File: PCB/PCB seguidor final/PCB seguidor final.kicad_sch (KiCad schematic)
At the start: 37 parts, among them J2 MOTOR A, J3 MOTOR B, J4 Conn_01x08, J6 Conn_01x04, SW1 SW_SPDT, U2 ESP32-DEVKIT-V1, U3 LM7805, U4 ROB-14450, U5 ROB-14450, U6 module_mpu6050

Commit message: las huellas FUNCIONAN
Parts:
- .1: footprint Connector:JWT_A3963_1x02_P3.96mm_Vertical -> Connector_AMASS:AMASS_XT30U-F_1x02_P5.0mm_Vertical
- R1, R2, R3, R4: footprint digikey-footprints:0603 -> digikey-kicad-library-master:0603
- U1, U7: footprint misc_footprints:MT3608_module -> MT3608:MT3608-Module

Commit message: Acabada(esperando corrección)
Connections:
- net +5V: now also GND1.3 (Pin_3)
- net +7.5V: now also SW1.1 (A)
- net BTN 1: now also U2.17 (VP); no longer U2.12 (RX0)
- net BTN 2: now also U2.12 (RX0); no longer U2.13 (TX0)
- net BTN 4: now also U2.13 (TX0); no longer U2.17 (VP)
- net MOTOR B1: now also U2.21 (D32); no longer U2.22 (D33)
- net MOTOR B2: now also U2.22 (D33); no longer U2.21 (D32)
- net VCC: no longer GND1.3 (Pin_3)
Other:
- moved on the sheet: .1
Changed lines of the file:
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@@
 	)
 	(junction
+		(at 88.9 83.82)
+		(diameter 0)
+		(color 0 0 0 0)
+	)
+	(junction
 		(at 250.19 105.41)
 		(diameter 0)
@@
 	(wire
 		(pts
-			(xy 252.73 107.95) (xy 257.81 107.95)
+			(xy 252.73 107.95) (xy 266.7 107.95)
 		)
 		(stroke
@@
 	(wire
 		(pts
+			(xy 88.9 81.28) (xy 88.9 83.82)
+		)
+		(stroke
+			(width 0)
+			(type default)
+		)
+	)
+	(wire
+		(pts
 			(xy 271.78 134.62) (xy 274.32 134.62)
 		)
@@
 	(wire
 		(pts
+			(xy 88.9 83.82) (xy 100.33 83.82)
+		)
+		(stroke
+			(width 0)
+			(type default)
+		)
+	)
+	(wire
+		(pts
 			(xy 67.31 40.64) (xy 67.31 44.45)
 		)
@@
 	(wire
 		(pts
-			(xy 250.19 105.41) (xy 257.81 105.41)
+			(xy 250.19 105.41) (xy 266.7 105.41)
 		)
 		(stroke
@@
 		)
 	)
-	(global_label "BTN 1"
+	(global_label "BTN 2"
 		(shape input)
 		(at 27.94 83.82 180)
@@
 		)
 	)
-	(global_label "BTN 2"
+	(global_label "BTN 4"
 		(shape input)
 		(at 27.94 86.36 180)
@@
 		)
 	)
-	(global_label "MOTOR B1"
+	(global_label "MOTOR B2"
 		(shape output)
 		(at 27.94 114.3 180)
@@
 		)
 	)
-	(global_label "MOTOR B2"
+	(global_label "MOTOR B1"
 		(shape output)
 		(at 27.94 111.76 180)
@@
 		)
 	)
-	(global_label "BTN 4"
+	(global_label "BTN 1"
 		(shape input)
 		(at 58.42 83.82 0)
@@
 		(on_board yes)
 		(dnp no)
-		(fields_autoplaced yes)
 		(property "Reference" "#PWR028"
 			(at 247.65 109.22 0)
@@
 		)
 		(property "Value" "+7.5V"
-			(at 247.65 100.33 0)
+			(at 247.396 101.6 0)
 			(effects
 				(font
 					(size 1.27 1.27)
 				)
+				(justify left)
 			)
 		)
@@
 	)
 	(symbol
+		(lib_id "power:+7.5V")
+		(at 88.9 83.82 0)
+		(unit 1)
+		(exclude_from_sim no)
+		(in_bom yes)
+		(on_board yes)
+		(dnp no)
+		(property "Reference" "#PWR030"
+			(at 88.9 87.63 0)
+			(effects
+				(font
+					(size 1.27 1.27)
+				)
+				(hide yes)
+			)
+		)
+		(property "Value" "+7.5V"
+			(at 88.646 80.01 0)
+			(effects
+				(font
+					(size 1.27 1.27)
+				)
+				(justify left)
+			)
+		)
+		(property "Footprint" ""
+			(at 88.9 83.82 0)
+			(effects
+				(font
+					(size 1.27 1.27)
+				)
+				(hide yes)
+			)
+		)
+		(property "Datasheet" ""
+			(at 88.9 83.82 0)
+			(effects
+				(font
+					(size 1.27 1.27)
+				)
+				(hide yes)
+			)
+		)
+		(property "Description" "Power symbol creates a global label with name \"+7.5V\""
+			(at 88.9 83.82 0)
+			(effects
+				(font
+					(size 1.27 1.27)
+				)
+				(hide yes)
+			)
+		)
+		(pin "1"
+		)
+		(instances
+			(project "PCB seguidor final"
+				(path "/e648e1de-53d7-47b7-8bc3-d4f3366b9377"
+					(reference "#PWR030")
+					(unit 1)
+				)
+			)
+		)
+	)
+	(symbol
 		(lib_id "ROB-14450:ROB-14450")
 		(at 46.99 41.91 0)
@@
 	(symbol
 		(lib_id "XT30PW-M:XT30PW-M")
-		(at 262.89 105.41 0)
+		(at 271.78 105.41 0)
 		(mirror y)
 		(unit 1)
@@
 		(dnp no)
 		(property "Reference" ".1"
-			(at 266.7 97.79 0)
+			(at 275.59 97.79 0)
 			(effects
 				(font
@@
 		)
 		(property "Value" "XT30PW-M"
-			(at 266.7 100.33 0)
+			(at 275.59 100.33 0)
 			(effects
 				(font
@@
 		)
 		(property "Footprint" "Connector_AMASS:AMASS_XT30U-F_1x02_P5.0mm_Vertical"
-			(at 262.89 105.41 0)
+			(at 271.78 105.41 0)
 			(effects
 				(font
@@
 		)
 		(property "Datasheet" ""
-			(at 262.89 105.41 0)
+			(at 271.78 105.41 0)
 			(effects
 				(font
@@
 		)
 		(property "Description" ""
-			(at 262.89 105.41 0)
+			(at 271.78 105.41 0)
 			(effects
 				(font
@@
 		)
 		(property "MF" "AMASS"
-			(at 262.89 105.41 0)
+			(at 271.78 105.41 0)
 			(effects
 				(font
@@
 		)
 		(property "MAXIMUM_PACKAGE_HEIGHT" "5 mm"
-			(at 262.89 105.41 0)
+			(at 271.78 105.41 0)
 			(effects
 				(font
@@
 		)
 		(property "Package" "None"
-			(at 262.89 105.41 0)
+			(at 271.78 105.41 0)
 			(effects
 				(font
@@
 		)
 		(property "Price" "None"
-			(at 262.89 105.41 0)
+			(at 271.78 105.41 0)
 			(effects
 				(font
@@
 		)
 		(property "Check_prices" "https://www.snapeda.com/parts/XT30PW-M/AMASS/view-part/?ref=eda"
-			(at 262.89 105.41 0)
+			(at 271.78 105.41 0)
 			(effects
 				(font
@@
 		)
 		(property "STANDARD" "Manufacturer Recommendations"
-			(at 262.89 105.41 0)
+			(at 271.78 105.41 0)
 			(effects
 				(font
@@
 		)
 		(property "PARTREV" "1.2"
-			(at 262.89 105.41 0)
+			(at 271.78 105.41 0)
 			(effects
 				(font
@@
 		)
 		(property "SnapEDA_Link" "https://www.snapeda.com/parts/XT30PW-M/AMASS/view-part/?ref=snap"
-			(at 262.89 105.41 0)
+			(at 271.78 105.41 0)
 			(effects
 				(font
@@
 		)
 		(property "MP" "XT30PW-M"
-			(at 262.89 105.41 0)
+			(at 271.78 105.41 0)
 			(effects
 				(font
@@
 		)
 		(property "Description_1" "\nSocket; DC supply; XT30; male; PIN: 2; on PCBs; THT; Colour: yellow\n"
-			(at 262.89 105.41 0)
+			(at 271.78 105.41 0)
 			(effects
 				(font
@@
 		)
 		(property "MANUFACTURER" "Amass"
-			(at 262.89 105.41 0)
+			(at 271.78 105.41 0)
 			(effects
 				(font
@@
 		)
 		(property "Availability" "Not in stock"
-			(at 262.89 105.41 0)
+			(at 271.78 105.41 0)
 			(effects
 				(font
@@
 		)
 		(property "SNAPEDA_PN" "XT30PW-M"
-			(at 262.89 105.41 0)
+			(at 271.78 105.41 0)
 			(effects
 				(font
@@
 		(on_board yes)
 		(dnp no)
-		(fields_autoplaced yes)
 		(property "Reference" "#PWR024"
 			(at 218.44 102.87 0)
@@
 			)
 		)
-		(property "Value" "VCC"
-			(at 210.82 102.87 90)
+		(property "Value" "+5V"
+			(at 207.264 102.616 90)
 			(effects
 				(font
 					(size 1.27 1.27)
 				)
-				(justify left)
+				(justify right)
 			)
 		)

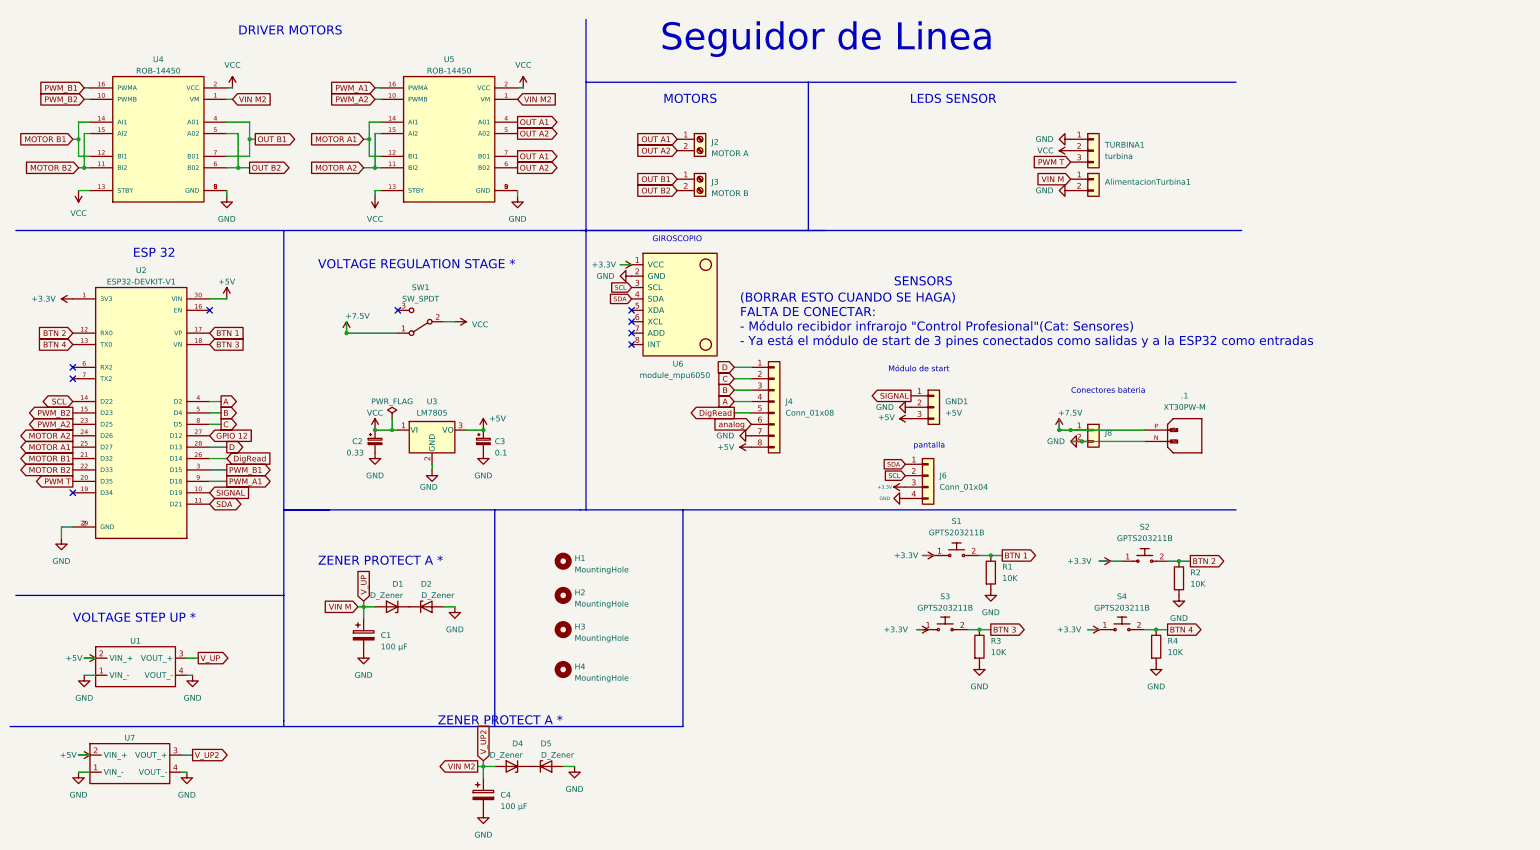
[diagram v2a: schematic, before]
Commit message: Algunas correcciones hechas
Flata poner led de encendido general y turbina, hacerla un poco mas estetica
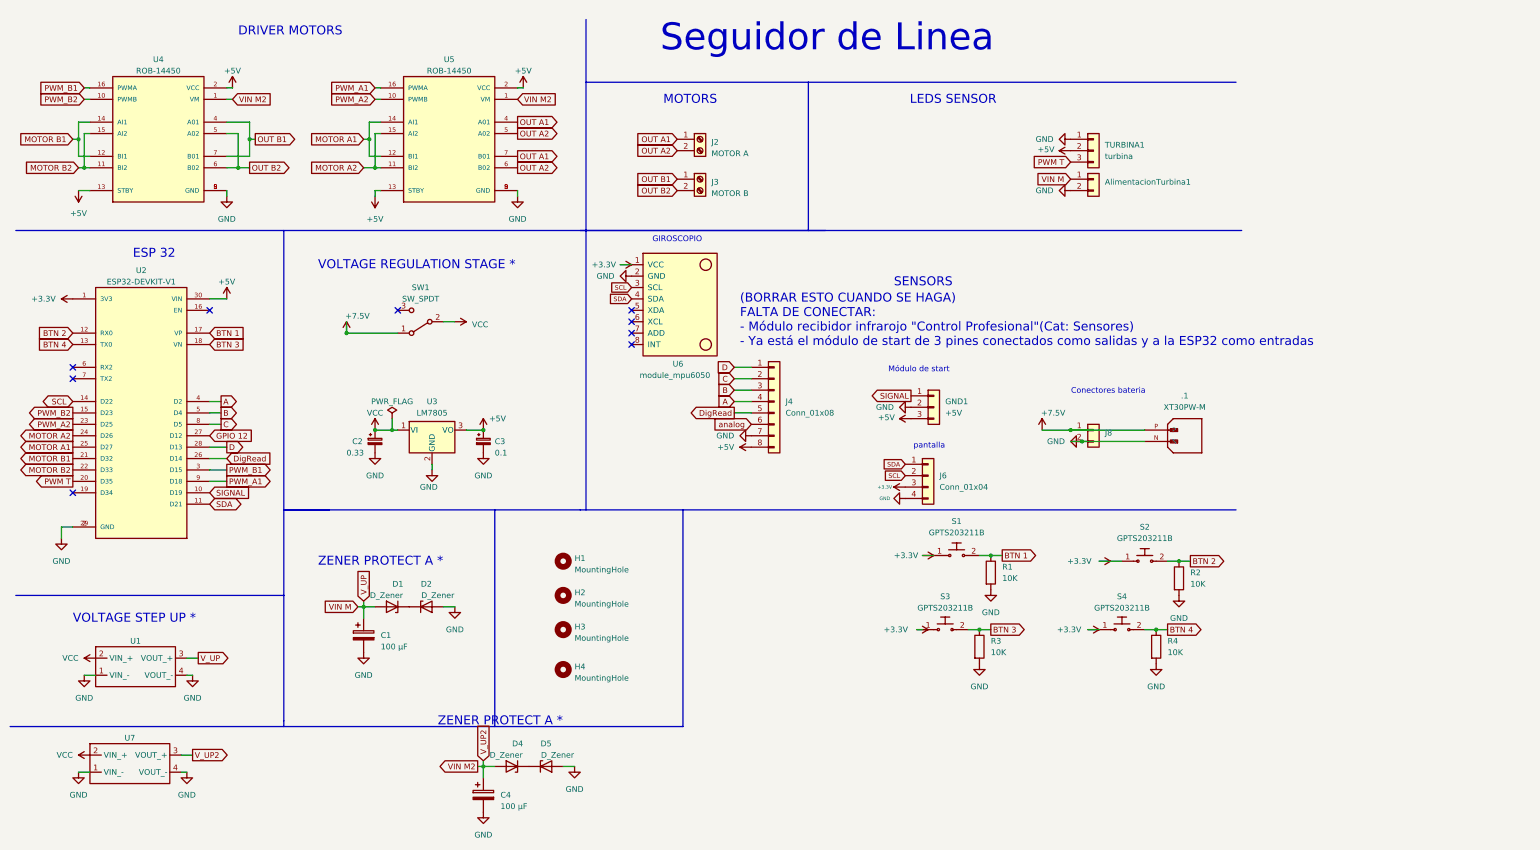
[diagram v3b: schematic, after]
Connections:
- net +5V: now also TURBINA1.2 (Pin_2), U4.13 (STBY), U4.2 (VCC), U5.13 (STBY), U5.2 (VCC); no longer U1.2 (VIN_+), U7.2 (VIN_+)
- net VCC: now also U1.2 (VIN_+), U7.2 (VIN_+); no longer TURBINA1.2 (Pin_2), U4.13 (STBY), U4.2 (VCC), U5.13 (STBY), U5.2 (VCC)

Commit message: Correcciones hechas
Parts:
- added D3, D6: LED, LED_SMD:LED_miniPLCC_2315_Handsoldering, symbol Device:LED
- added R5, R6: 10K, digikey-kicad-library-master:0603, symbol Device:R
- added SW2: SW_SPDT, Connector_PinHeader_2.54mm:PinHeader_1x03_P2.54mm_Vertical, symbol Switch:SW_SPDT
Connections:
- net +5V: now also R5.2
- net GND: now also D3.1 (K), D6.1 (K)
- net VCC: now also SW2.1 (A); no longer U1.2 (VIN_+)
- new net: D3.2 (A), R5.1
- new net: D6.2 (A), R6.1
- new net Ve: R6.2, SW2.2 (B), U1.2 (VIN_+)
- no-connect marks 9 -> 10
